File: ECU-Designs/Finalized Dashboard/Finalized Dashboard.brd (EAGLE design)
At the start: 93.4 x 83.3 mm, 41 parts, among them X1 MINIFIT_5566-4, X2 MINIFIT_5566-2, X5 MINIFIT_5566-4

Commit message: Dashboard
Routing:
- net 12V: track 153.7 -> 209.4 mm
- net N$9: track 23.7 -> 22.0 mm
- net CAN-L: track 272.9 -> 273.5 mm
- net 5V: vias 4 -> 5
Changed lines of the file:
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@@
 <wire x1="46.482" y1="16.256" x2="53.916" y2="16.256" width="0.4064" layer="16"/>
 <wire x1="53.916" y1="16.256" x2="53.916" y2="13.672" width="0.4064" layer="16"/>
-<wire x1="13.276" y1="26.372" x2="17.018" y2="26.372" width="0.4064" layer="16"/>
-<wire x1="17.018" y1="26.372" x2="17.018" y2="25.908" width="0.4064" layer="16"/>
-<via x="17.018" y="25.908" extent="1-16" drill="0.6" shape="square"/>
-<wire x1="17.018" y1="25.908" x2="28.702" y2="25.908" width="0.4064" layer="1"/>
-<wire x1="28.702" y1="25.908" x2="28.702" y2="18.796" width="0.4064" layer="1"/>
-<wire x1="28.702" y1="18.796" x2="42.926" y2="18.796" width="0.4064" layer="1"/>
-<wire x1="42.926" y1="18.796" x2="42.926" y2="13.97" width="0.4064" layer="1"/>
+<wire x1="13.276" y1="26.372" x2="16.256" y2="26.372" width="0.4064" layer="16"/>
+<wire x1="16.256" y1="26.372" x2="16.256" y2="25.908" width="0.4064" layer="16"/>
+<via x="16.256" y="25.908" extent="1-16" drill="0.6" shape="square"/>
+<wire x1="16.256" y1="25.908" x2="28.702" y2="25.908" width="0.4064" layer="1"/>
+<wire x1="28.702" y1="25.908" x2="28.702" y2="18.288" width="0.4064" layer="1"/>
+<wire x1="28.702" y1="18.288" x2="42.926" y2="18.288" width="0.4064" layer="1"/>
+<wire x1="42.926" y1="18.288" x2="42.926" y2="13.97" width="0.4064" layer="1"/>
 <via x="42.926" y="13.97" extent="1-16" drill="0.6" shape="square"/>
 <wire x1="42.926" y1="13.97" x2="42.926" y2="11.938" width="0.4064" layer="16"/>
@@
 <wire x1="85.09" y1="71.628" x2="85.09" y2="43.688" width="0.4064" layer="1"/>
 <via x="85.09" y="43.688" extent="1-16" drill="0.6" shape="square"/>
-<wire x1="85.09" y1="43.688" x2="81.788" y2="43.688" width="0.4064" layer="16"/>
-<via x="81.788" y="43.688" extent="1-16" drill="0.6" shape="square"/>
-<wire x1="81.788" y1="43.688" x2="80.772" y2="43.688" width="0.4064" layer="1"/>
+<wire x1="85.09" y1="43.688" x2="80.518" y2="43.688" width="0.4064" layer="16"/>
+<via x="80.518" y="43.688" extent="1-16" drill="0.6" shape="square"/>
+<wire x1="80.518" y1="43.688" x2="80.772" y2="43.688" width="0.4064" layer="1"/>
 <contactref element="R17" pad="P$1"/>
 <wire x1="42.926" y1="4.318" x2="51.816" y2="4.318" width="0.4064" layer="16"/>
 <wire x1="9.076" y1="26.372" x2="10.922" y2="26.372" width="0.4064" layer="16"/>
 <wire x1="10.922" y1="26.372" x2="10.922" y2="28.702" width="0.4064" layer="16"/>
-<wire x1="10.922" y1="28.702" x2="18.288" y2="28.702" width="0.4064" layer="16"/>
-<wire x1="18.288" y1="28.702" x2="18.288" y2="18.034" width="0.4064" layer="16"/>
-<via x="18.288" y="18.034" extent="1-16" drill="0.6" shape="square"/>
-<wire x1="18.288" y1="18.034" x2="24.638" y2="18.034" width="0.4064" layer="1"/>
+<wire x1="10.922" y1="28.702" x2="17.78" y2="28.702" width="0.4064" layer="16"/>
+<wire x1="17.78" y1="28.702" x2="17.78" y2="18.034" width="0.4064" layer="16"/>
+<via x="17.78" y="18.034" extent="1-16" drill="0.6" shape="square"/>
+<wire x1="17.78" y1="18.034" x2="24.638" y2="18.034" width="0.4064" layer="1"/>
 <wire x1="24.638" y1="18.034" x2="24.638" y2="17.018" width="0.4064" layer="1"/>
 <wire x1="24.638" y1="17.018" x2="40.386" y2="17.018" width="0.4064" layer="1"/>
@@
 <wire x1="64.964" y1="46.355" x2="62.992" y2="46.355" width="0.4064" layer="1"/>
 <wire x1="62.992" y1="46.355" x2="62.992" y2="46.99" width="0.4064" layer="1"/>
-<wire x1="62.992" y1="46.99" x2="50.038" y2="46.99" width="0.4064" layer="1"/>
-<wire x1="50.038" y1="46.99" x2="50.038" y2="43.18" width="0.4064" layer="1"/>
+<wire x1="62.992" y1="46.99" x2="52.324" y2="46.99" width="0.4064" layer="1"/>
+<wire x1="52.324" y1="46.99" x2="50.038" y2="43.18" width="0.4064" layer="1"/>
 <via x="50.038" y="43.18" extent="1-16" drill="0.6" shape="square"/>
 <wire x1="50.038" y1="43.18" x2="45.72" y2="43.18" width="0.4064" layer="16"/>
@@
 <wire x1="12.954" y1="20.872" x2="12.954" y2="17.526" width="0.4064" layer="16"/>
 <wire x1="12.954" y1="17.526" x2="9.652" y2="17.526" width="0.4064" layer="16"/>
-<wire x1="9.652" y1="17.526" x2="9.652" y2="1.27" width="0.4064" layer="16"/>
+<wire x1="9.652" y1="17.526" x2="9.652" y2="16.256" width="0.4064" layer="16"/>
+<wire x1="9.652" y1="15.748" x2="9.652" y2="1.27" width="0.4064" layer="16"/>
 <wire x1="9.652" y1="1.27" x2="13.462" y2="1.27" width="0.4064" layer="16"/>
 <wire x1="12.954" y1="20.872" x2="12.954" y2="23.114" width="0.4064" layer="16"/>
@@
 <wire x1="6.858" y1="32.512" x2="8.28" y2="32.512" width="0.4064" layer="16"/>
 <wire x1="8.28" y1="32.512" x2="8.28" y2="32.498" width="0.4064" layer="16"/>
-<wire x1="8.28" y1="32.498" x2="7.62" y2="55.118" width="0" layer="19" extent="16-16"/>
+<wire x1="7.62" y1="55.118" x2="0.254" y2="55.118" width="0.4064" layer="16"/>
+<wire x1="0.254" y1="55.118" x2="0.254" y2="16.256" width="0.4064" layer="16"/>
+<wire x1="0.254" y1="16.256" x2="9.652" y2="16.256" width="0.4064" layer="16"/>
+<wire x1="9.652" y1="16.256" x2="9.652" y2="15.748" width="0.4064" layer="16"/>
 </signal>
 <signal name="N$41">
@@
 <contactref element="C1" pad="1"/>
 <wire x1="2.54" y1="30.988" x2="2.54" y2="37.084" width="0.4064" layer="16"/>
+<via x="54.102" y="44.45" extent="1-16" drill="0.6" shape="square"/>
 </signal>
 <signal name="N$13">

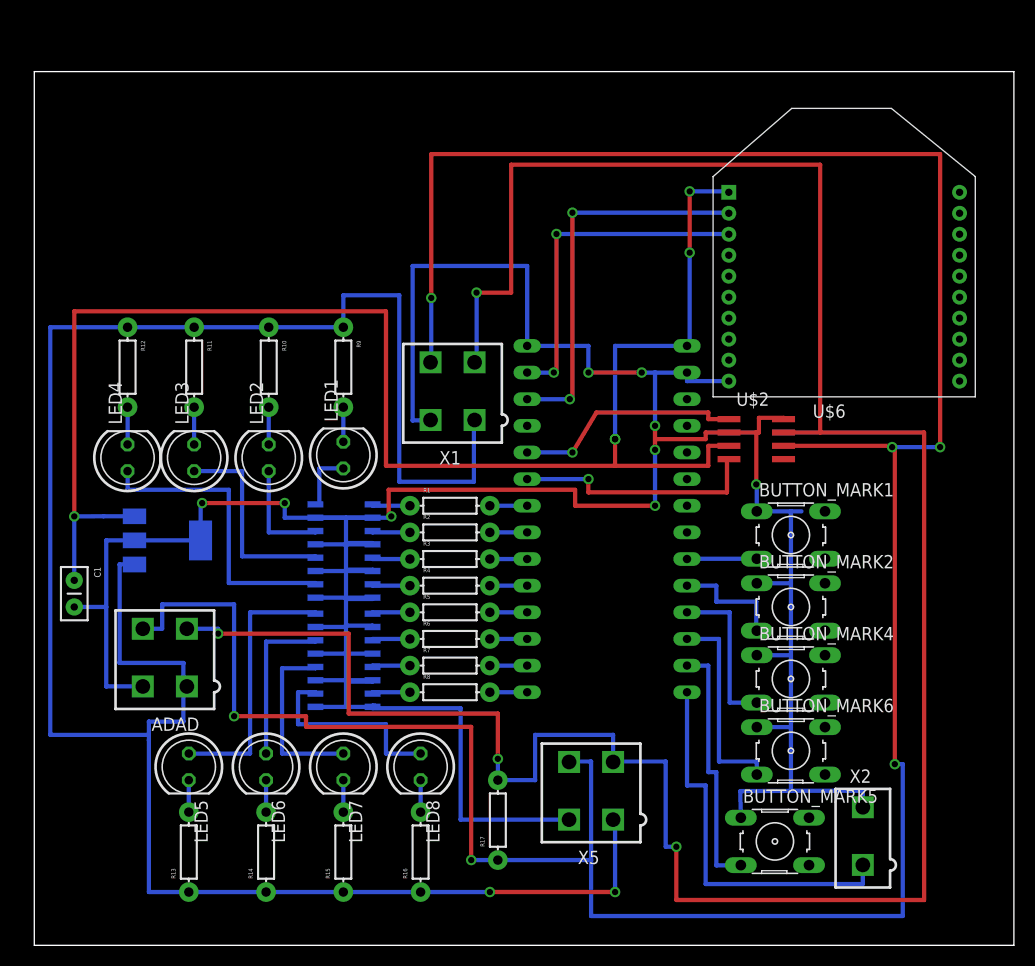
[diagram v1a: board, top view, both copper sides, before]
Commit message: Dashboard without Xbee
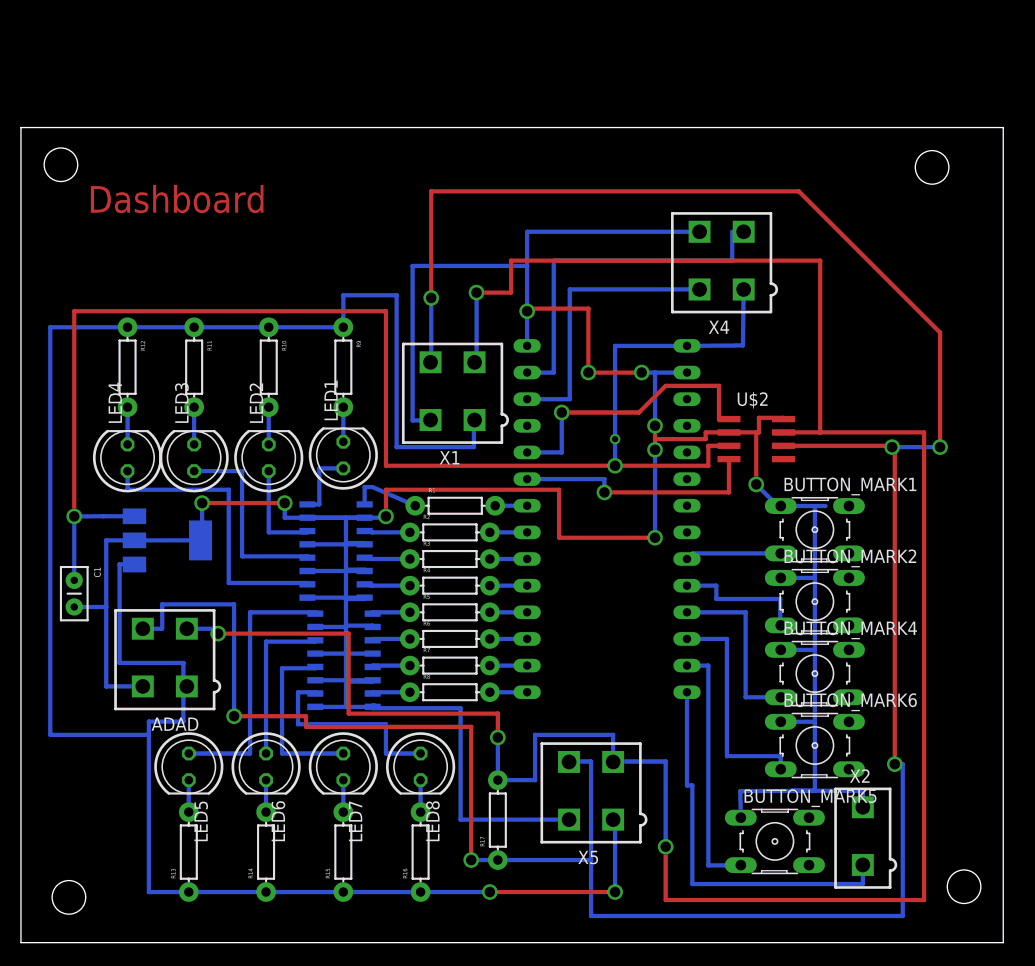
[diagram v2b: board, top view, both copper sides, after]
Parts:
- removed U$6: XBEE, HyTechDevices:XBEE
- added X4: MINIFIT_5566-4, HyTechDevices:MINIFIT_5566-4
- moved BUTTON_MARK1 2.34 mm to (73.2, 35.8)
- moved BUTTON_MARK6 2.34 mm to (73.2, 15.2)
- moved BUTTON_MARK2 2.34 mm to (73.2, 29.0)
- moved BUTTON_MARK4 2.34 mm to (73.2, 22.1)
- moved U$4 0.76 mm to (27.4, 33.8)
- moved R1 0.51 mm to (38.9, 38.1)
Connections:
- net 5V: now also X4.1; no longer U$6.1
- net GND: now also X4.4; no longer U$6.10
- net N$13: now also X4.3; no longer U$6.3
- net N$2: now also X4.2; no longer U$6.2
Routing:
- net GND: track 333.5 -> 361.2 mm, vias 9 -> 10
- net CAN-H: track 240.2 -> 221.9 mm
- net CAN-L: track 273.5 -> 258.5 mm
- net N$2: track 37.1 -> 26.9 mm, vias 2 -> 0
- net 5V: track 147.5 -> 139.7 mm, vias 5 -> 3
- net 12V: track 209.4 -> 202.8 mm
- net N$9: track 22.0 -> 27.3 mm
- net N$5: track 3.68 -> 6.85 mm
- net N$42: track 6.68 -> 9.19 mm
- net N$45: track 19.6 -> 21.4 mm
- net N$44: track 15.3 -> 17.0 mm
- net N$43: track 10.9 -> 12.7 mm
- net N$13: track 32.5 -> 34.1 mm, vias 2 -> 0
- net N$28: track 28.7 -> 27.9 mm
- net N$27: track 19.8 -> 19.1 mm
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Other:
- board size 93.4 x 83.3 mm -> 93.7 x 77.7 mm
- board text added: "Dashboard"

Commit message: Massive Commit
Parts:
- added LED10, LED11, LED12, LED13, LED14, LED15, LED16, LED17, LED18, LED9: WS2812B5050, HyTechDevices:RGBLED5050
- added R18: (no value), HyTechDevices:AXIAL-0.3
- moved R12 2.50 mm to (6.60, 53.6)
- moved R10 2.29 mm to (21.1, 53.6)
- moved R11 2.29 mm to (14.0, 53.6)
- moved R9 2.29 mm to (28.2, 53.6)
- moved LED4 2.05 mm to (6.60, 44.5), turned to 270 degrees
- moved LED2 2.03 mm to (21.1, 44.7), turned to 270 degrees
- moved LED3 1.78 mm to (14.0, 44.5), turned to 270 degrees
- moved LED1 1.52 mm to (28.2, 44.5), turned to 270 degrees
- moved R13 1.02 mm to (13.5, 4.06)
- moved R14 1.02 mm to (20.8, 4.06)
- moved R15 1.02 mm to (28.2, 4.06)
- moved R16 1.02 mm to (35.6, 4.06)
- moved LED5 0.51 mm to (13.5, 12.7), turned to 90 degrees
- moved LED6 0.51 mm to (20.8, 12.7), turned to 90 degrees
- moved LED7 0.51 mm to (28.2, 12.7), turned to 90 degrees
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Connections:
- new net N$1: LED10.3, LED9.6
- new net N$18: LED12.6, LED13.3
- new net N$3: LED10.6, LED11.3
- new net N$4: LED11.6, LED12.3
- new net N$48: LED14.6, LED15.3
- new net N$49: LED15.6, LED16.3
- new net N$50: LED16.6, LED17.3
- new net N$51: LED17.6, LED18.3
- new net N$52: C1.1, R18.P$1, U$1.VIN, U$2.3, U$3.3, X4.1
- new net N$53: LED9.3, U$1.D2
- new net N$6: LED13.6, LED14.3
- net 5V: now also LED10.4, LED11.4, LED12.4, LED13.4, LED14.4, LED15.4, LED16.4, LED17.4, LED18.4, LED9.4, R18.P$2; no longer C1.1, U$1.VIN, U$2.3, U$3.3, X4.1
- net GND: now also LED10.1, LED11.1, LED12.1, LED13.1, LED14.1, LED15.1, LED16.1, LED17.1, LED18.1, LED9.1
- net N$25: now also R9.P$2; no longer U$4.16
- net N$26: now also R10.P$2; no longer U$4.14
- net N$27: now also R11.P$2; no longer U$4.12
- net N$28: now also R12.P$2; no longer U$4.10
- net N$29: now also R13.P$2; no longer U$5.16
- net N$30: now also R14.P$2; no longer U$5.14
- net N$31: now also R15.P$2; no longer U$5.12
- net N$32: now also R16.P$2; no longer U$5.10
- net N$33: now also U$4.16; no longer R9.P$2
- net N$34: now also U$4.14; no longer R10.P$2
- net N$35: now also U$4.12; no longer R11.P$2
- net N$36: now also U$4.10; no longer R12.P$2
- net N$37: now also U$5.16; no longer R13.P$2
- net N$38: now also U$5.14; no longer R14.P$2
- net N$39: now also U$5.12; no longer R15.P$2
- net N$40: now also U$5.10; no longer R16.P$2
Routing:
- net N$52: track 0.00 -> 153.9 mm, vias 0 -> 3
- net GND: track 361.2 -> 507.7 mm, vias 10 -> 11
- net N$53: track 0.00 -> 91.9 mm, vias 0 -> 3
- net 5V: track 139.7 -> 107.1 mm, vias 3 -> 0
- net N$36: track 3.56 -> 30.7 mm
- net N$28: track 27.9 -> 4.06 mm
- net N$37: track 3.05 -> 25.9 mm
- net N$29: track 25.7 -> 3.56 mm
- net N$35: track 3.56 -> 20.8 mm
- net N$40: track 3.05 -> 19.6 mm
- net N$32: track 19.3 -> 3.56 mm
- net N$1: track 0.00 -> 15.2 mm
- net N$3: track 0.00 -> 15.1 mm
- net N$27: track 19.1 -> 4.06 mm
- net N$39: track 3.05 -> 17.3 mm
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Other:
- board size 93.7 x 77.7 mm -> 93.7 x 87.9 mm
